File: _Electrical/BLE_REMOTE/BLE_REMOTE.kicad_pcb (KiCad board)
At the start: 4 copper layers, 48.2 x 23.1 mm, 66 parts, among them J2 Display, J3 PGRM, J4 Conn_01x02_Pin, J5 Conn_01x02_Pin, J6 Conn_01x02_Pin, J7 Conn_01x02_Pin, J8 Conn_01x02_Pin, J9 Conn_01x02_Pin, Q1 NPN, Q2 SSM3K35AMFVL3FCT-ND, Q3 SSM3J35AMFVL3FCT-ND, U1 MIC5528-3.3YMX-TR, U3 BQ24232RGTR, U4 MCP65R41, U5 nRF52832-QFxx, Y2 Crystal_GND24

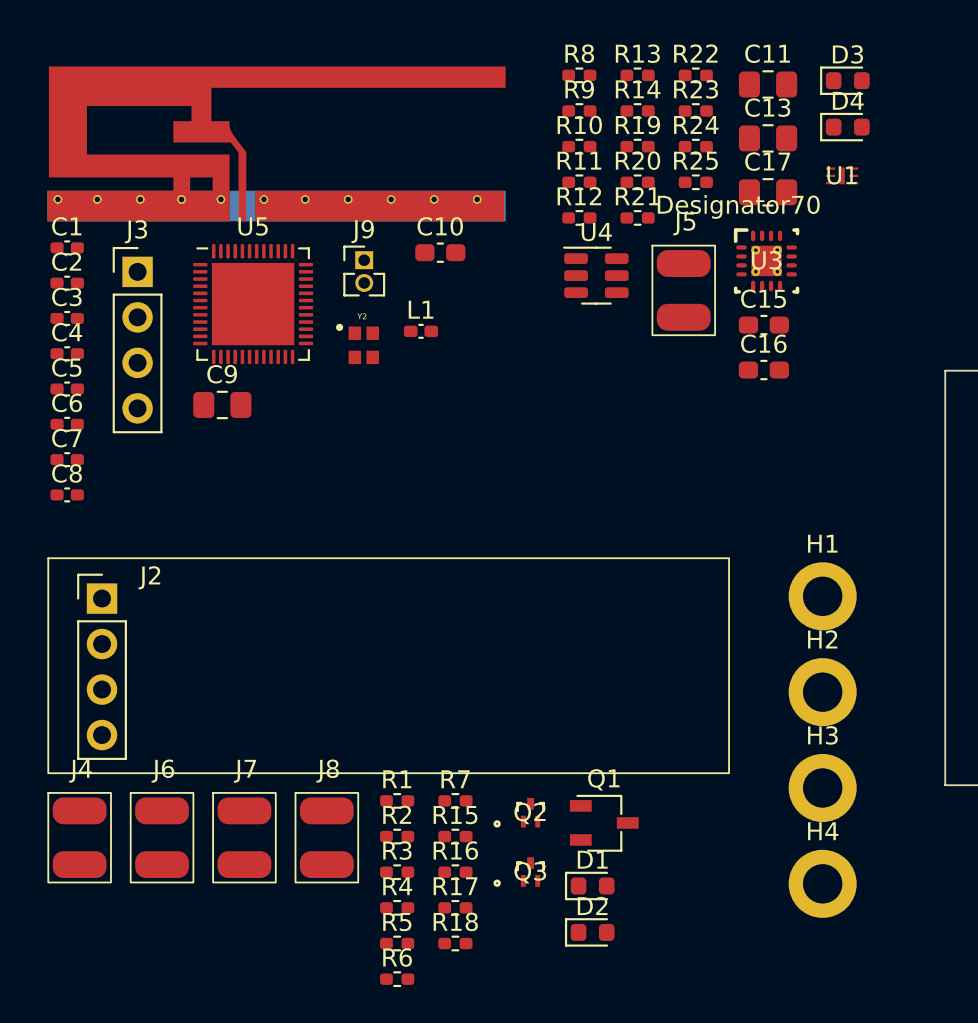
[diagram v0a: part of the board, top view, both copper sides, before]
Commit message: Added simulation and updated power button
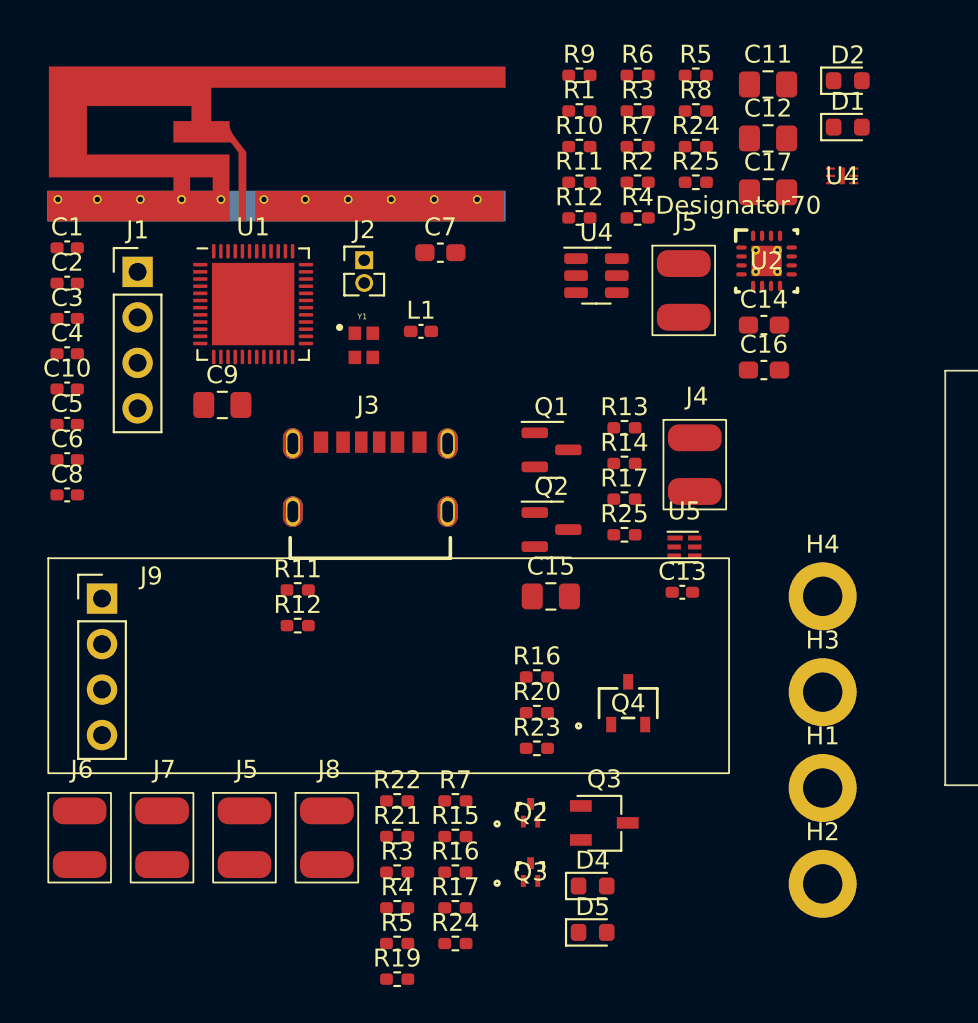
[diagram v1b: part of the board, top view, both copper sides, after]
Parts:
- added C13: 0.1uF, Capacitor_SMD:C_0402_1005Metric_Pad0.74x0.62mm_HandSolder, F.Cu at (167.9, 124.4)
- added C15: 4.7uF, Capacitor_SMD:C_0805_2012Metric_Pad1.18x1.45mm_HandSolder, F.Cu at (160.6, 124.7)
- added J3: USBC, _Parts:GCT_USB4125-GF-A_REVA2, F.Cu at (150.5, 119.1)
- added J4: Battery, _Parts:2pad_conn_sm, F.Cu at (168.6, 117.3)
- added Q1: IRLML6244, Package_TO_SOT_SMD:SOT-23, F.Cu at (160.6, 116.5)
- added Q2: IRLML6244, Package_TO_SOT_SMD:SOT-23, F.Cu at (160.6, 120.9)
- added Q4: BSS806NEH6327XTSA1, _Parts:PG-SOT23-3-5_INF, F.Cu at (164.9, 130.6)
- added R11: 2k, Resistor_SMD:R_0402_1005Metric_Pad0.72x0.64mm_HandSolder, F.Cu at (146.5, 124.3)
- added R12: 2k, Resistor_SMD:R_0402_1005Metric_Pad0.72x0.64mm_HandSolder, F.Cu at (146.5, 126.3)
- added R13: 47k, Resistor_SMD:R_0402_1005Metric_Pad0.72x0.64mm_HandSolder, F.Cu at (164.7, 115.3)
- added R14: 330, Resistor_SMD:R_0402_1005Metric_Pad0.72x0.64mm_HandSolder, F.Cu at (164.7, 117.3)
- added R16: 47k, Resistor_SMD:R_0402_1005Metric_Pad0.72x0.64mm_HandSolder, F.Cu at (159.8, 129.2)
- added R17: 47k, Resistor_SMD:R_0402_1005Metric_Pad0.72x0.64mm_HandSolder, F.Cu at (164.7, 119.2)
- added R20: 2k, Resistor_SMD:R_0402_1005Metric_Pad0.72x0.64mm_HandSolder, F.Cu at (159.8, 131.2)
- added R23: 47k, Resistor_SMD:R_0402_1005Metric_Pad0.72x0.64mm_HandSolder, F.Cu at (159.8, 133.2)
- added R25: 2.2K, Resistor_SMD:R_0402_1005Metric_Pad0.72x0.64mm_HandSolder, F.Cu at (164.7, 121.2)
- added U5: BQ297xy, Package_SON:WSON-6_1.5x1.5mm_P0.5mm, F.Cu at (168.1, 121.9)
- J8: value Conn_01x02_Pin -> Buzzer
- R19: renamed from R6; value 1k -> 2k
- renumbered C5 to C10, C13 to C12, C15 to C14, C6 to C5, C7 to C6, C10 to C7, D4 to D1, D3 to D2, D1 to D4, D2 to D5, H3 to H1, H4 to H2, H2 to H3, H1 to H4, J3 to J1, J9 to J2, J7 to J5, J4 to J6, J6 to J7, J2 to J9, Q1 to Q3, R9 to R1, R20 to R2, R2 to R21, R1 to R22, R18 to R24, R14 to R3, R21 to R4, R22 to R5, R13 to R6, R19 to R7, R23 to R8, R8 to R9, U5 to U1, U3 to U2, U1 to U4, Y2 to Y1
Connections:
- D1 pad 1: /Power/CHG_N -> CHG_N
- D1 pad 2: Net-(D4-A) -> Net-(D1-A)
- D2 pad 1: /Power/PGOOD_N -> PGOOD_N
- D2 pad 2: Net-(D3-A) -> Net-(D2-A)
- D4 pad 2: Net-(D1-A) -> Net-(D4-A)
- D5 pad 2: Net-(D2-A) -> Net-(D5-A)
- R19 pad 2: Net-(D1-A) -> Net-(D4-A)
- U1 pad 4: unconnected-(U5-P0.02/AIN0-Pad4) -> TEST_BAT
- U1 pad 8: unconnected-(U5-P0.06-Pad8) -> CHG_N
- U1 pad 9: unconnected-(U5-P0.07-Pad9) -> PGOOD_N
- U2 pad 2: /Power/VBAT -> /Power/Battery/VBAT
- U2 pad 3: /Power/VBAT -> /Power/Battery/VBAT
- U2 pad 7: /Power/PGOOD_N -> PGOOD_N
- U2 pad 9: /Power/CHG_N -> CHG_N

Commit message: started PCB design
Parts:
- removed the J5 at (143.5, 138.1)
- removed the J5 at (168.0, 107.6)
- removed the Q2 at (160.6, 120.9)
- removed the Q2 at (159.5, 136.7)
- removed the Q3 at (159.5, 140.1)
- removed the Q3 at (163.6, 137.3)
- removed Q4: BSS806NEH6327XTSA1, _Parts:PG-SOT23-3-5_INF
- removed the R11 at (146.5, 124.3)
- removed the R11 at (162.2, 101.6)
- removed the R12 at (146.5, 126.3)
- removed the R12 at (162.2, 103.5)
- removed the R16 at (155.3, 140.1)
- removed the R16 at (159.8, 129.2)
- removed the R17 at (164.7, 119.2)
- removed the R17 at (155.3, 142.1)
- removed the R24 at (168.7, 99.6)
- removed the R24 at (155.3, 144.0)
- removed the R25 at (168.7, 101.6)
- removed the R25 at (164.7, 121.2)
- removed the R3 at (165.4, 97.6)
- removed the R3 at (152.0, 140.1)
- removed the R4 at (165.4, 103.5)
- removed the R4 at (152.0, 142.1)
- removed the R5 at (152.0, 144.0)
- removed the R5 at (168.7, 95.6)
- removed the R7 at (165.4, 99.6)
- removed the R7 at (155.3, 136.1)
- removed the U4 at (163.1, 106.8)
- removed the U4 at (176.9, 101.2)
- added C18: 4.7uF, Capacitor_SMD:C_0805_2012Metric_Pad1.18x1.45mm_HandSolder, F.Cu at (159.8, 156.2)
- added D3: LED, LED_SMD:LED_0603_1608Metric, F.Cu at (134.6, 95.1)
- added J5: Conn_01x02_Pin, _Parts:2pad_conn_sm, F.Cu at (162.8, 124.7)
- added Q2: NPN, Package_TO_SOT_SMD:TSOT-23, F.Cu at (161.9, 137.2)
- added Q3: PMOS, Package_TO_SOT_SMD:SOT-323_SC-70_Handsoldering, F.Cu at (166.9, 155.2)
- added R11: 2k, Resistor_SMD:R_0402_1005Metric_Pad0.72x0.64mm_HandSolder, F.Cu at (143.1, 114.8)
- added R12: 2k, Resistor_SMD:R_0402_1005Metric_Pad0.72x0.64mm_HandSolder, F.Cu at (143.1, 116.7)
- added R16: 220, Resistor_SMD:R_0402_1005Metric_Pad0.72x0.64mm_HandSolder, F.Cu at (125.1, 100.8)
- added R17: 1k, Resistor_SMD:R_0402_1005Metric_Pad0.72x0.64mm_HandSolder, F.Cu at (125.1, 102.8)
- added R18: 47k, Resistor_SMD:R_0402_1005Metric_Pad0.72x0.64mm_HandSolder, F.Cu at (125.1, 104.8)
- added R24: 173k, Resistor_SMD:R_0402_1005Metric_Pad0.72x0.64mm_HandSolder, F.Cu at (143.1, 174.3)
- added R25: 100k, Resistor_SMD:R_0402_1005Metric_Pad0.72x0.64mm_HandSolder, F.Cu at (143.1, 176.3)
- added R26: 100k, Resistor_SMD:R_0402_1005Metric_Pad0.72x0.64mm_HandSolder, F.Cu at (143.1, 178.3)
- added R27: 10k, Resistor_SMD:R_0402_1005Metric_Pad0.72x0.64mm_HandSolder, F.Cu at (143.1, 180.3)
- added R3: 0R, Resistor_SMD:R_0402_1005Metric_Pad0.72x0.64mm_HandSolder, F.Cu at (139.8, 114.8)
- added R4: 0R, Resistor_SMD:R_0402_1005Metric_Pad0.72x0.64mm_HandSolder, F.Cu at (139.8, 116.7)
- added R5: 0R, Resistor_SMD:R_0402_1005Metric_Pad0.72x0.64mm_HandSolder, F.Cu at (139.8, 118.7)
- added R7: 4.32k, Resistor_SMD:R_0402_1005Metric_Pad0.72x0.64mm_HandSolder, F.Cu at (143.1, 110.8)
- added SW1: SW_Push, Button_Switch_SMD:SW_Push_1P1T_NO_6x6mm_H9.5mm, F.Cu at (180.6, 157.7)
- added U3: MIC5528-3.3YMX-TR, _Parts:XTDFN6_1P2X1P2_MCH, F.Cu at (175.4, 144.8)
- added U4: MCP65R41, Package_TO_SOT_SMD:SOT-23-6, F.Cu at (172.5, 157.7)
- C13: value 0.1uF -> 2.2uF; footprint Capacitor_SMD:C_0402_1005Metric_Pad0.74x0.62mm_HandSolder -> Capacitor_SMD:C_0603_1608Metric_Pad1.08x0.95mm_HandSolder
- C15: value 4.7uF -> 10uF; footprint Capacitor_SMD:C_0805_2012Metric_Pad1.18x1.45mm_HandSolder -> Capacitor_SMD:C_0402_1005Metric_Pad0.74x0.62mm_HandSolder
- C16: value 2.2uF -> 0.1uF; footprint Capacitor_SMD:C_0603_1608Metric_Pad1.08x0.95mm_HandSolder -> Capacitor_SMD:C_0402_1005Metric_Pad0.74x0.62mm_HandSolder
- C17: value 4.7uF -> 1uF; footprint Capacitor_SMD:C_0805_2012Metric_Pad1.18x1.45mm_HandSolder -> Capacitor_SMD:C_0402_1005Metric_Pad0.74x0.62mm_HandSolder
- D5: value LED -> 1N4148WX-TP; footprint LED_SMD:LED_0603_1608Metric -> _Parts:CR_SOD323_MCC-L
- J4: value Battery -> Conn_01x02_Pin
- J7: value Conn_01x02_Pin -> Buzzer
- J8: value Buzzer -> Display; footprint _Parts:2pad_conn_sm -> _Parts:OLED_091
- J9: value Display -> Battery; footprint _Parts:OLED_091 -> _Parts:2pad_conn_sm
- Q1: value IRLML6244 -> BSS806NEH6327XTSA1; footprint Package_TO_SOT_SMD:SOT-23 -> _Parts:PG-SOT23-3-5_INF
- R13: value 47k -> 2k
- R14: value 330 -> 2k
- R19: value 2k -> 47k
- R20: value 2k -> 100k
- R21: value 220 -> 100k
- R22: value 1k -> 300k
- R23: value 47k -> 1k
- R6: value 5.1k -> 0R
- R8: value 0R -> 5.1k
- R9: value 4.32k -> 5.1k
- U5: value BQ297xy -> IRF7319TRPBF; footprint Package_SON:WSON-6_1.5x1.5mm_P0.5mm -> _Parts:TRANS_IRF7103TRPBF_INF
- moved C17 79.3 mm to (146.3, 176.9)
- moved J8 68.5 mm to (201.4, 95.2), turned to 180 degrees
- moved C16 68.2 mm to (146.3, 175.0)
- moved A1 68.0 mm to (194.9, 145.9), turned to -90 degrees
- moved C1 64.2 mm to (188.5, 138.5), turned to 90 degrees
- moved C3 63.5 mm to (187.1, 143.5), turned to 90 degrees
- moved J1 61.4 mm to (178.1, 152.7), turned to 90 degrees
- moved J2 61.3 mm to (189.2, 153.2), turned to 180 degrees
- moved C2 60.4 mm to (185.2, 138.6), turned to 90 degrees
- moved C5 60.3 mm to (187.6, 141.7)
- moved C6 59.0 mm to (187.6, 140.8)
- moved C8 53.9 mm to (183.8, 138.6), turned to -90 degrees
- moved C4 53.1 mm to (177.2, 141.4), turned to 180 degrees
- moved C10 52.3 mm to (179.2, 138.8), turned to -90 degrees
- moved U1 51.8 mm to (182.0, 143.5)
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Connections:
- net Net-(U2-ILIM) renamed /Power/BQ_ILIM
- C13 pad 1: Net-(U5-BAT) -> VCC
- C13 pad 2: /Power/Battery/BAT- -> GND
- C14 pad 1: VCC -> VDD
- C15 pad 2: /Power/Battery/BAT- -> Net-(U5-G1)
- C16 pad 1: VDD -> /Power/Battery/BAT+
- C16 pad 2: GND -> Net-(U5-G2)
- C17 pad 1: /Power/VBAT -> Net-(U5-G2)
- C17 pad 2: GND -> Net-(D5-K)
- D5 pad 1: GND -> Net-(D5-K)
- D5 pad 2: Net-(D5-A) -> /Power/Battery/BAT_CTRL
- J4 pad 1: /Power/Battery/BAT- -> GND
- J4 pad 2: /Power/Battery/VBAT -> SWITCH
- J6 pad 2: TEST -> BUTTON
- J7 pad 1: GND -> Net-(J7-Pin_1)
- J7 pad 2: BUTTON -> VCC
- J8 pad 1: Net-(J8-Pin_1) -> DIS_SDA
- J8 pad 2: VCC -> DIS_SCL
- J9 pad 1: DIS_SDA -> /Power/Battery/BAT-
- J9 pad 2: DIS_SCL -> /Power/Battery/BAT+
- Q1 pad 1: Net-(Q1-G) -> VCC
- Q1 pad 2: GND -> DIS_EN
- Q1 pad 3: Net-(Q1-D) -> /Peripherals/DIS_PWR
- R13 pad 1: GND -> VDD
- R13 pad 2: TEST_BAT -> Net-(D3-A)
- R14 pad 1: /Power/Battery/VBAT -> USER
- R14 pad 2: Net-(U5-BAT) -> Net-(D4-A)
- R15 pad 1: VCC -> GND
- R15 pad 2: Net-(Q2-G) -> DIS_EN
- R19 pad 1: VDD -> DIS_SCL
- R19 pad 2: Net-(D4-A) -> VDD
- R20 pad 1: USER -> /Power/Battery/VBAT
- R20 pad 2: Net-(D5-A) -> /Power/Battery/BAT_CTRL
- R21 pad 1: BUZZ -> Net-(U4-+)
- R22 pad 1: VCC -> /Power/Battery/BAT_CTRL
- R22 pad 2: Net-(J8-Pin_1) -> Net-(U5-G1)
- R23 pad 1: DIS_SDA -> TEST_BAT
- R23 pad 2: VDD -> Net-(U4-+)
- R6 pad 1: GND -> /Power/BQ_TMR
- R6 pad 2: Net-(J3-CC2) -> GND
- R8 pad 1: /Power/BQ_TMR -> GND
- R8 pad 2: GND -> Net-(J3-CC1)
- R9 pad 2: Net-(U2-ISET) -> Net-(J3-CC2)
- U2 pad 16: Net-(U2-ISET) -> /Power/BQ_ISET
- U5 pad 1: unconnected-(U5-NC-Pad1) -> GND
- U5 pad 2: Net-(Q1-G) -> Net-(U5-G1)
- U5 pad 3: Net-(Q2-G) -> /Power/Battery/BAT+
- U5 pad 4: /Power/Battery/BAT- -> Net-(U5-G2)
- U5 pad 5: Net-(U5-BAT) -> /Power/Battery/VBAT
- U5 pad 6: Net-(U5-V-) -> /Power/Battery/VBAT
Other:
- board size 48.2 x 23.1 mm -> 49.5 x 30.5 mm
- board text removed: "+"
- board text removed: "BAT"
- board text removed: "BTN"
- board text removed: "BZZ"
- board text removed: "By:MSE Date:01/12/23 Rev:2"
- board text removed: "SWT"
- board text removed: "TST"
- board text removed: "_"

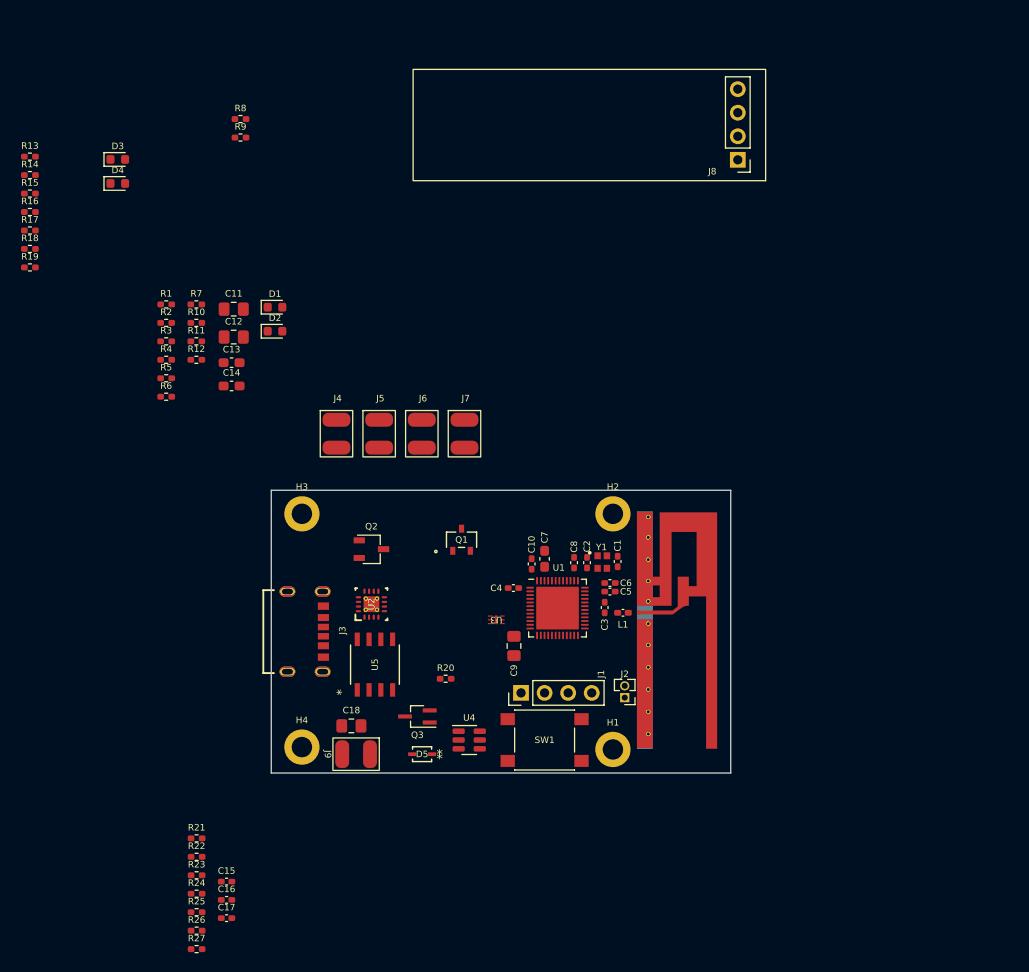
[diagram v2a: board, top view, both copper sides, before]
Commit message: PCB parts placed
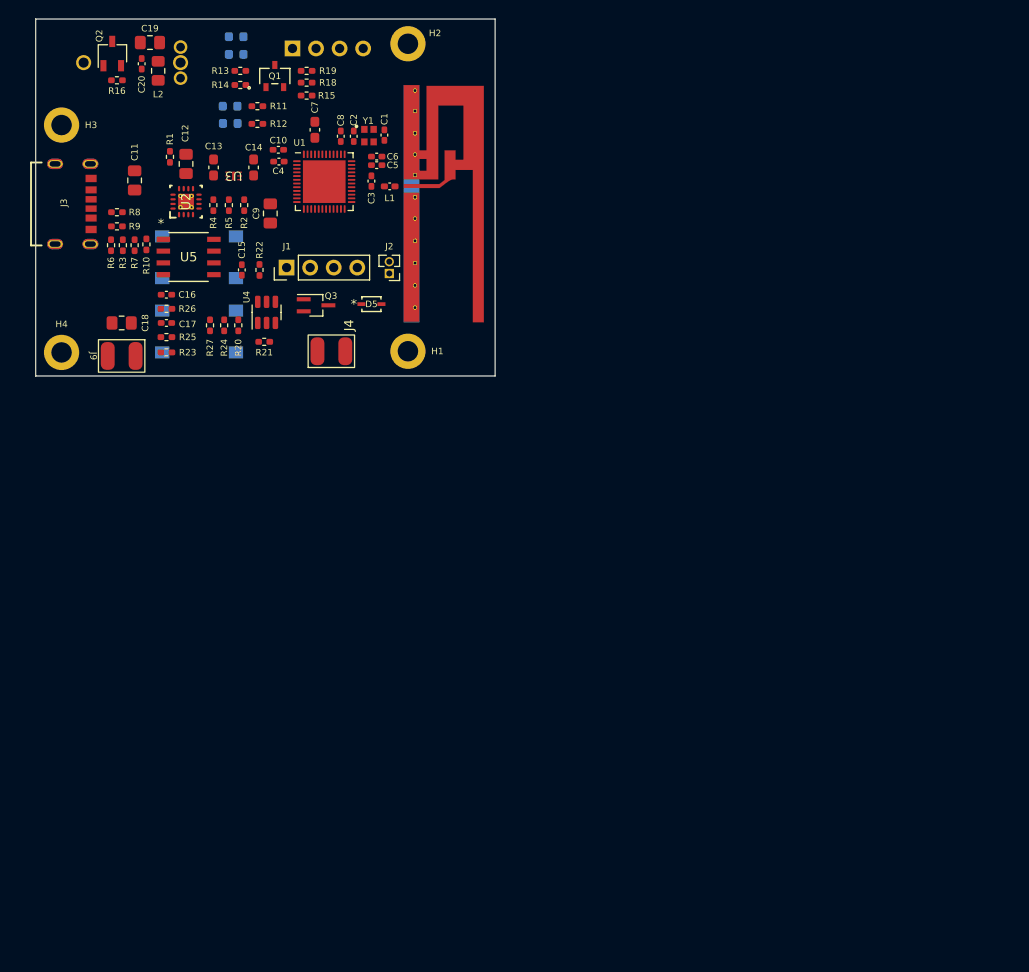
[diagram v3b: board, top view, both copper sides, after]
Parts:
- removed J5, J6: Conn_01x02_Pin, _Parts:2pad_conn_sm
- removed J7: Buzzer, _Parts:2pad_conn_sm
- removed R17: 1k, Resistor_SMD:R_0402_1005Metric_Pad0.72x0.64mm_HandSolder
- added C19: 4.7uF, Capacitor_SMD:C_0805_2012Metric_Pad1.18x1.45mm_HandSolder, F.Cu at (138.0, 82.5)
- added C20: 1nF, Capacitor_SMD:C_0402_1005Metric_Pad0.74x0.62mm_HandSolder, F.Cu at (137.2, 84.8)
- added L2: 10uH, Inductor_SMD:L_0805_2012Metric_Pad1.15x1.40mm_HandSolder, F.Cu at (138.9, 85.6)
- added SW3: SW_Push, Button_Switch_SMD:SW_Push_1P1T_NO_6x6mm_H9.5mm, B.Cu at (143.3, 105.7)
- added U6: 316040005, _Parts:316040005, B.Cu at (130.9, 84.7)
- D1, D2, D3, D4, J8, SW1: moved to B.Cu
- J4: value Conn_01x02_Pin -> SWITCH
- moved R27 67.3 mm to (144.5, 113.0), turned to 90 degrees
- moved R26 67.1 mm to (139.8, 111.3)
- moved C15 66.0 mm to (148.0, 107.1), turned to 90 degrees
- moved C16 65.6 mm to (139.8, 109.7), turned to 180 degrees
- moved C17 64.5 mm to (139.8, 112.8)
- moved R22 63.6 mm to (149.9, 107.1), turned to -90 degrees
- moved R25 62.1 mm to (139.8, 114.3), turned to 180 degrees
- moved R24 61.3 mm to (146.1, 113.0), turned to -90 degrees
- moved Q2 60.3 mm to (134.0, 83.7), turned to 90 degrees
- moved SW1 57.7 mm to (143.3, 113.7), turned to 180 degrees
- moved R23 56.5 mm to (139.8, 116.0)
- moved U3 55.6 mm to (147.1, 96.9)
- moved H2 55.3 mm to (165.9, 82.7)
- moved R21 54.0 mm to (150.4, 114.8), turned to 180 degrees
- moved Q1 53.9 mm to (151.5, 86.2)
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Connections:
- R3 pad 1: /Power/BQ_EN1 -> /Power/BQ_ITERM
- R4 pad 1: /Power/BQ_ITERM -> /Power/BQ_CE_N
- U2 pad 15: /Power/BQ_EN1 -> /Power/BQ_ITERM
- U2 pad 4: /Power/BQ_ITERM -> /Power/BQ_CE_N
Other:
- board size 49.5 x 30.5 mm -> 49.5 x 38.5 mm
